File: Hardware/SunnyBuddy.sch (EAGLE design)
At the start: 33 parts, among them J1 5.5x2.1mm Barrel, J3 POWER_JACKPTH, J5 M02PTH, J6 M023.5MM, J7 M023.5MM, J8 M023.5MM, U1 LT3652

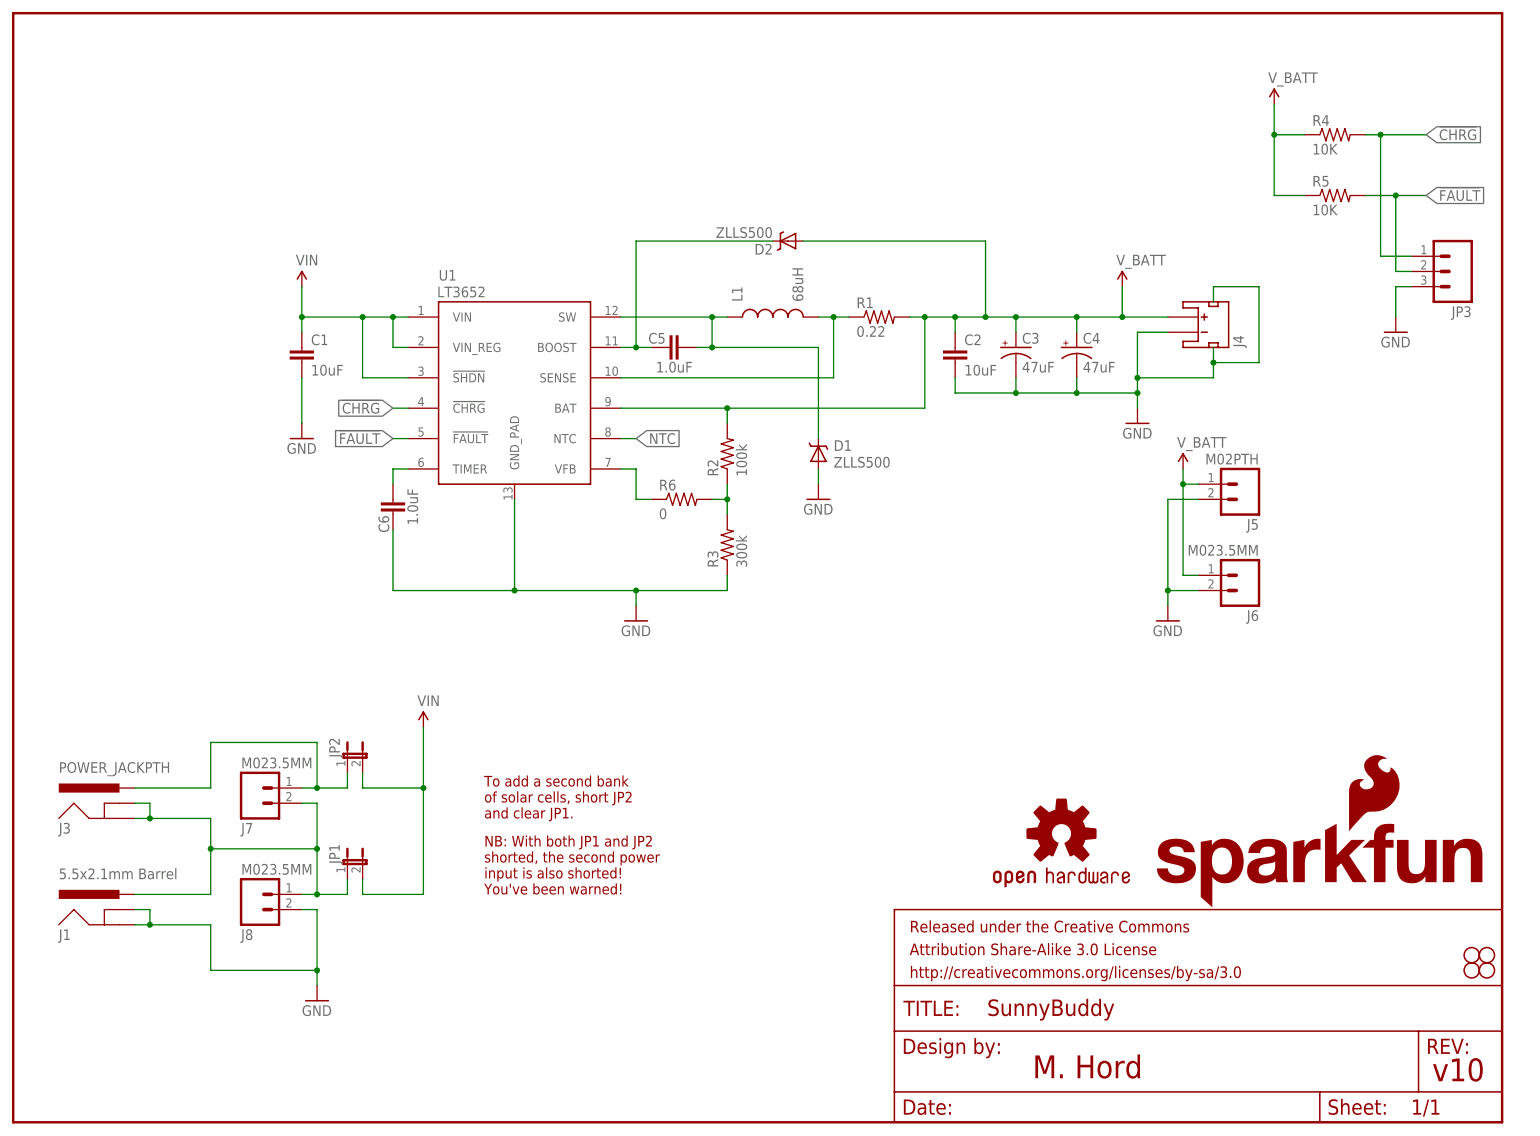
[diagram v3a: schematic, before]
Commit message: Add trimpot, adjust output res values
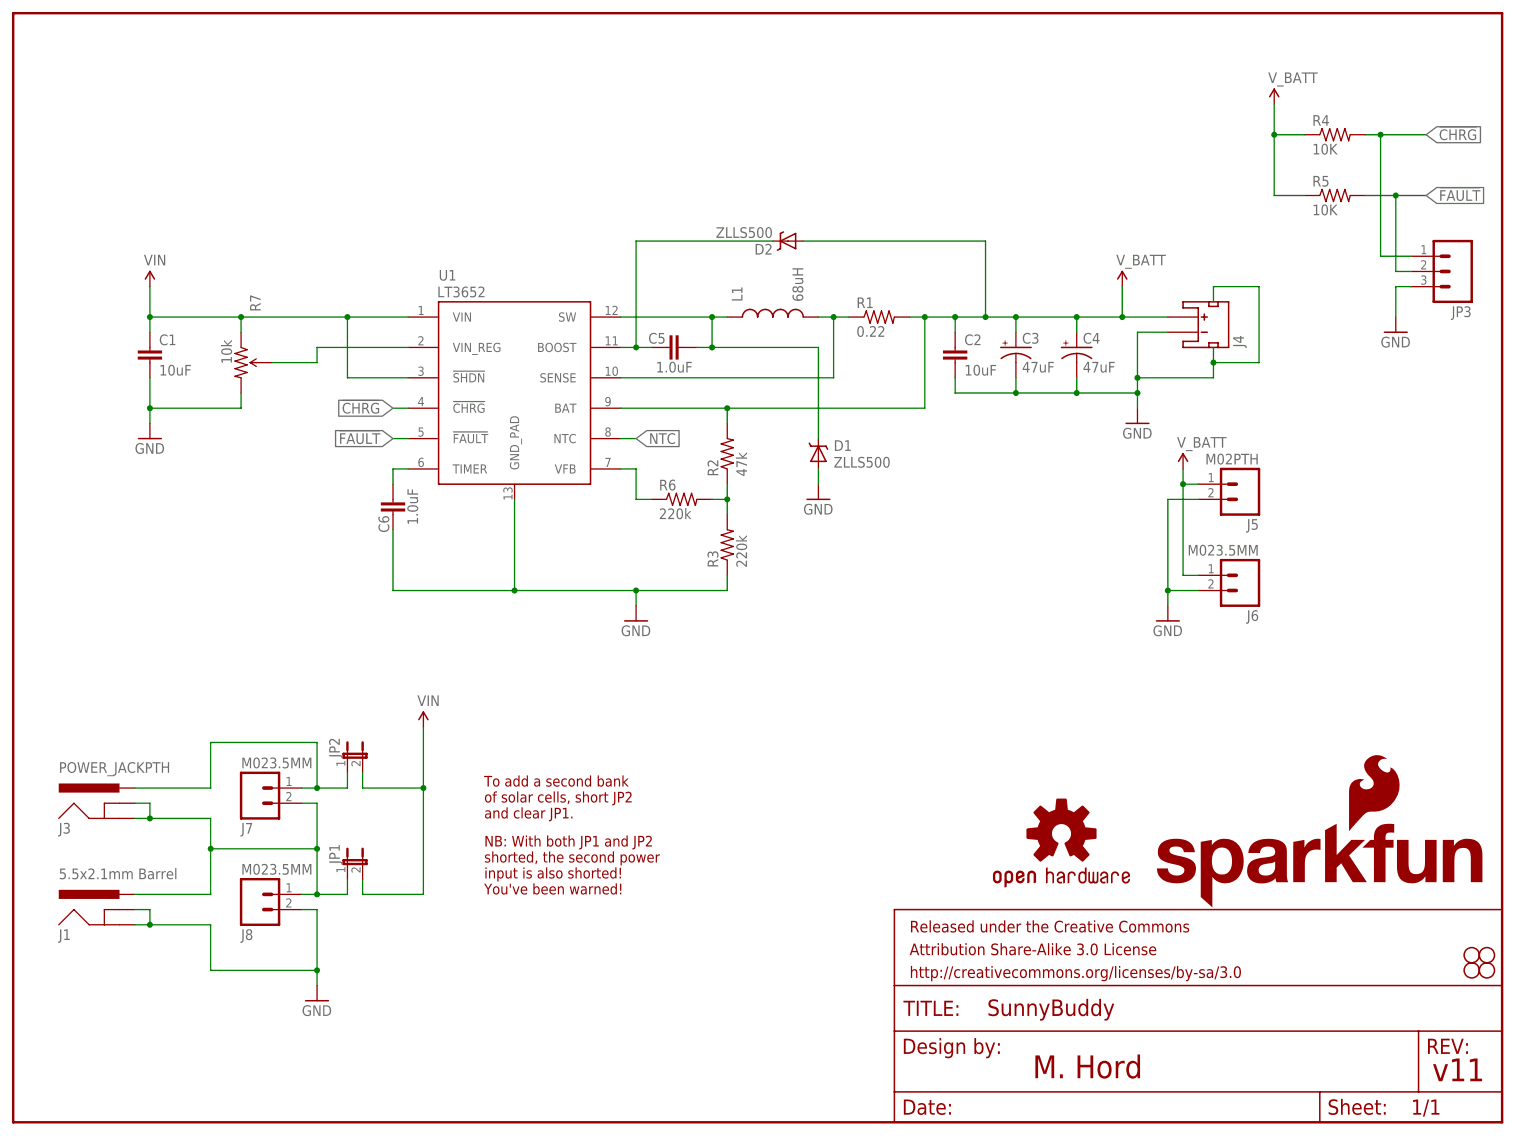
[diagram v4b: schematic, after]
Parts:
- added R7: 10k, SparkFun-Electromechanical:TRIMPOTRES-09285
- R2: value 100k -> 47k; device SparkFun-Resistors:100KOHM1/10W1%(0603) -> SparkFun-Resistors:47KOHM1/10W1%(0603)
- R3: value 300k -> 220k; device SparkFun-Resistors:300KOHM-1/10W-1%(0603) -> SparkFun-Resistors:220KOHM1/10W1%(0603)
- R6: value 0 -> 220k; device SparkFun-Resistors:0OHM1/10W5%(0603) -> SparkFun-Resistors:220KOHM1/10W1%(0603)
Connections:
- new net N$4: R7.WIPER, U1.VIN_REG
- net GND: now also R7.CW
- net VIN: now also R7.CCW; no longer U1.VIN_REG
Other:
- note added: "v11"
- note removed: "v10"
- moved on the sheet: C1
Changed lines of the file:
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@@
 <part name="C6" library="SparkFun-Capacitors" deviceset="1.0UF-16V-10%(0603)" device="" value="1.0uF"/>
 <part name="GND4" library="SparkFun-Aesthetics" deviceset="GND" device=""/>
-<part name="R3" library="SparkFun-Resistors" deviceset="300KOHM-1/10W-1%(0603)" device="" value="300k"/>
-<part name="R2" library="SparkFun-Resistors" deviceset="100KOHM1/10W1%(0603)" device="" value="100k"/>
+<part name="R3" library="SparkFun-Resistors" deviceset="220KOHM1/10W1%(0603)" device="" value="220k"/>
+<part name="R2" library="SparkFun-Resistors" deviceset="47KOHM1/10W1%(0603)" device="" value="47k"/>
 <part name="J5" library="SparkFun-Connectors" deviceset="M02" device="PTH"/>
 <part name="J6" library="SparkFun-Connectors" deviceset="M02" device="3.5MM"/>
@@
 <part name="JP3" library="SparkFun-Connectors" deviceset="M03" device="PTH"/>
 <part name="GND7" library="SparkFun-Aesthetics" deviceset="GND" device=""/>
-<part name="R6" library="SparkFun-Resistors" deviceset="0OHM1/10W5%(0603)" device="" value="0"/>
+<part name="R6" library="SparkFun-Resistors" deviceset="220KOHM1/10W1%(0603)" device="" value="220k"/>
+<part name="R7" library="SparkFun-Electromechanical" deviceset="TRIMPOT" device="RES-09285" value="10k"/>
 </parts>
 <sheets>
@@
 input is also shorted!
 You've been warned!</text>
-<text x="237.236" y="6.858" size="3.81" layer="94">v10</text>
+<text x="237.236" y="6.858" size="3.81" layer="94">v11</text>
 <text x="170.434" y="7.366" size="3.81" layer="94">M. Hord</text>
 </plain>
@@
 <instance part="U1" gate="G$1" x="71.12" y="106.68"/>
 <instance part="R1" gate="G$1" x="144.78" y="134.62"/>
-<instance part="C1" gate="G$1" x="48.26" y="127"/>
+<instance part="C1" gate="G$1" x="22.86" y="127"/>
 <instance part="C3" gate="G$1" x="167.64" y="129.54"/>
 <instance part="C4" gate="G$1" x="177.8" y="129.54"/>
@@
 <instance part="D2" gate="G$1" x="129.54" y="147.32" rot="R180"/>
 <instance part="SUPPLY1" gate="G$1" x="185.42" y="139.7"/>
-<instance part="SUPPLY2" gate="G$1" x="48.26" y="139.7"/>
-<instance part="GND1" gate="1" x="48.26" y="114.3"/>
+<instance part="SUPPLY2" gate="G$1" x="22.86" y="139.7"/>
+<instance part="GND1" gate="1" x="22.86" y="114.3"/>
 <instance part="GND2" gate="1" x="187.96" y="116.84"/>
 <instance part="C5" gate="G$1" x="111.76" y="129.54" smashed="yes" rot="R90">
@@
 <instance part="GND7" gate="1" x="231.14" y="132.08"/>
 <instance part="R6" gate="G$1" x="111.76" y="104.14"/>
+<instance part="R7" gate="R?" x="38.1" y="127" rot="R270"/>
 </instances>
 <busses>
@@
 <pinref part="C1" gate="G$1" pin="1"/>
 <pinref part="U1" gate="G$1" pin="VIN"/>
-<wire x1="63.5" y1="134.62" x2="66.04" y2="134.62" width="0.1524" layer="91"/>
-<pinref part="U1" gate="G$1" pin="VIN_REG"/>
-<wire x1="66.04" y1="129.54" x2="63.5" y2="129.54" width="0.1524" layer="91"/>
-<wire x1="63.5" y1="129.54" x2="63.5" y2="134.62" width="0.1524" layer="91"/>
-<junction x="63.5" y="134.62"/>
-<wire x1="58.42" y1="134.62" x2="63.5" y2="134.62" width="0.1524" layer="91"/>
+<wire x1="55.88" y1="134.62" x2="66.04" y2="134.62" width="0.1524" layer="91"/>
 <pinref part="U1" gate="G$1" pin="!SHDN"/>
-<wire x1="66.04" y1="124.46" x2="58.42" y2="124.46" width="0.1524" layer="91"/>
-<wire x1="58.42" y1="124.46" x2="58.42" y2="134.62" width="0.1524" layer="91"/>
-<junction x="58.42" y="134.62"/>
+<wire x1="66.04" y1="124.46" x2="55.88" y2="124.46" width="0.1524" layer="91"/>
+<wire x1="55.88" y1="124.46" x2="55.88" y2="134.62" width="0.1524" layer="91"/>
+<junction x="55.88" y="134.62"/>
 <pinref part="SUPPLY2" gate="G$1" pin="VIN"/>
-<wire x1="48.26" y1="139.7" x2="48.26" y2="134.62" width="0.1524" layer="91"/>
-<wire x1="48.26" y1="134.62" x2="58.42" y2="134.62" width="0.1524" layer="91"/>
-<junction x="48.26" y="134.62"/>
-<wire x1="48.26" y1="134.62" x2="48.26" y2="132.08" width="0.1524" layer="91"/>
+<wire x1="22.86" y1="139.7" x2="22.86" y2="134.62" width="0.1524" layer="91"/>
+<wire x1="22.86" y1="134.62" x2="38.1" y2="134.62" width="0.1524" layer="91"/>
+<junction x="22.86" y="134.62"/>
+<wire x1="38.1" y1="134.62" x2="55.88" y2="134.62" width="0.1524" layer="91"/>
+<wire x1="22.86" y1="134.62" x2="22.86" y2="132.08" width="0.1524" layer="91"/>
+<pinref part="R7" gate="R?" pin="CCW"/>
+<wire x1="38.1" y1="132.08" x2="38.1" y2="134.62" width="0.1524" layer="91"/>
+<junction x="38.1" y="134.62"/>
 </segment>
 <segment>
@@
 <pinref part="GND1" gate="1" pin="GND"/>
 <pinref part="C1" gate="G$1" pin="2"/>
-<wire x1="48.26" y1="116.84" x2="48.26" y2="124.46" width="0.1524" layer="91"/>
+<wire x1="22.86" y1="116.84" x2="22.86" y2="119.38" width="0.1524" layer="91"/>
+<pinref part="R7" gate="R?" pin="CW"/>
+<wire x1="22.86" y1="119.38" x2="22.86" y2="124.46" width="0.1524" layer="91"/>
+<wire x1="38.1" y1="121.92" x2="38.1" y2="119.38" width="0.1524" layer="91"/>
+<wire x1="38.1" y1="119.38" x2="22.86" y2="119.38" width="0.1524" layer="91"/>
+<junction x="22.86" y="119.38"/>
 </segment>
 <segment>
@@
 </segment>
 </net>
+<net name="N$4" class="0">
+<segment>
+<pinref part="U1" gate="G$1" pin="VIN_REG"/>
+<pinref part="R7" gate="R?" pin="WIPER"/>
+<wire x1="43.18" y1="127" x2="50.8" y2="127" width="0.1524" layer="91"/>
+<wire x1="50.8" y1="127" x2="50.8" y2="129.54" width="0.1524" layer="91"/>
+<wire x1="50.8" y1="129.54" x2="66.04" y2="129.54" width="0.1524" layer="91"/>
+</segment>
+</net>

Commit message: Add current sense jumper, set V node, Fritzing
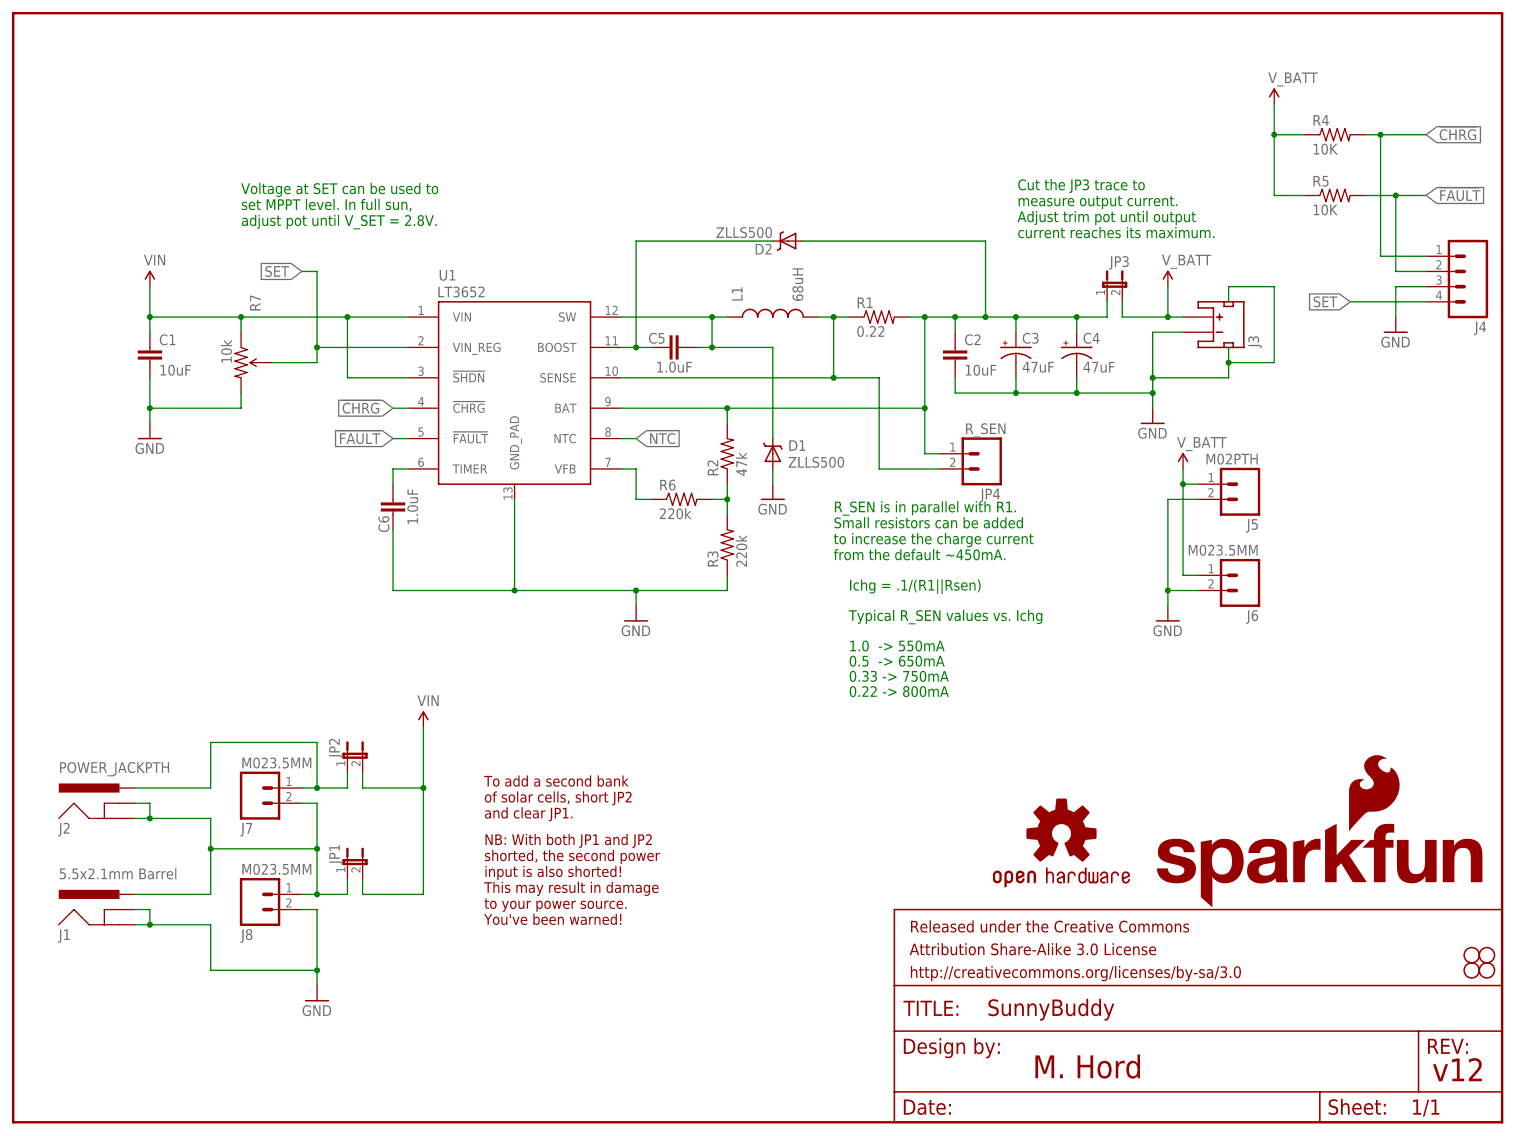
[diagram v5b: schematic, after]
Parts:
- added J2: POWER_JACKPTH, SparkFun-Connectors:POWER_JACKPTH
- added JP4: R_SEN, SparkFun-Connectors:M02PTH
- J3: value POWER_JACKPTH -> (none); device SparkFun-Connectors:POWER_JACKPTH -> SparkFun-Connectors:JST_2MM_MALE
- J4: device SparkFun-Connectors:JST_2MM_MALE -> SparkFun-Connectors:M04PTH
- JP3: value (none) -> JUMPER-PTH-2-NC; device SparkFun-Connectors:M03PTH -> SparkFun-Passives:JUMPER-PTH-2-NC
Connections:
- new net SET: J4.4, R7.WIPER, U1.VIN_REG
- net !CHRG: now also J4.1; no longer JP3.1
- net !FAULT: now also J4.2; no longer JP3.2
- net GND: now also J3.-, J3.PAD1, J3.PAD2, J4.3; no longer J4.-, J4.PAD1, J4.PAD2, JP3.3
- net N$4: now also C2.1, C3.+, C4.+, D2.A, JP3.1, JP4.1, R1.2, R2.2, U1.BAT; no longer R7.WIPER, U1.VIN_REG
- net N$8: now also J2.GND, J2.GNDBREAK; no longer J3.GND, J3.GNDBREAK
- net SENSE: now also JP4.2
- net SFSASDF: now also J2.PWR; no longer J3.PWR
- net V_BATT: now also J3.+, JP3.2; no longer C2.1, C3.+, C4.+, D2.A, J4.+, R1.2, R2.2, U1.BAT
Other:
- note added: "0.22 -> 800mA"
- note added: "0.33 -> 750mA"
- note added: "0.5 -> 650mA"
- note added: "1.0 -> 550mA"
- note added: "Cut the JP3 trace to measure output current. Adjust trim pot until output current reaches its maximum."
- note added: "Ichg = .1/(R1||Rsen)"
- note added: "NB: With both JP1 and JP2 shorted, the second power input is also shorted! This may result in damage to your power source. You've been warned!"
- note added: "R_SEN is in parallel with R1. Small resistors can be added to increase the charge current from the default ~450mA."
- note added: "Typical R_SEN values vs. Ichg"
- note added: "Voltage at SET can be used to set MPPT level. In full sun, adjust pot until V_SET = 2.8V."
- note added: "v12"
- note removed: "NB: With both JP1 and JP2 shorted, the second power input is also shorted! You've been warned!"
- note removed: "v11"
- moved on the sheet: D1
